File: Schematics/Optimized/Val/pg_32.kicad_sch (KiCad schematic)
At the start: 15 parts, among them U23 F04, U24 XALU32, U25 XALU32, U26 F51, U27 PA010, U30 PA011, U33 F04, U3607 F86, U3608 F04, U3613 F30, U3614 F30, U3615 F00, U3616 F04, U3617 F20, U3619 F20

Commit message: Polish
Tested: passed expmon_test_{typ,val} (-busmux)
Tested: passed run_udiag on r2000
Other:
- moved on the sheet: U23, U24, U25, U26, U27, U30, U33, U3607, U3608, U3613, U3614, U3615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

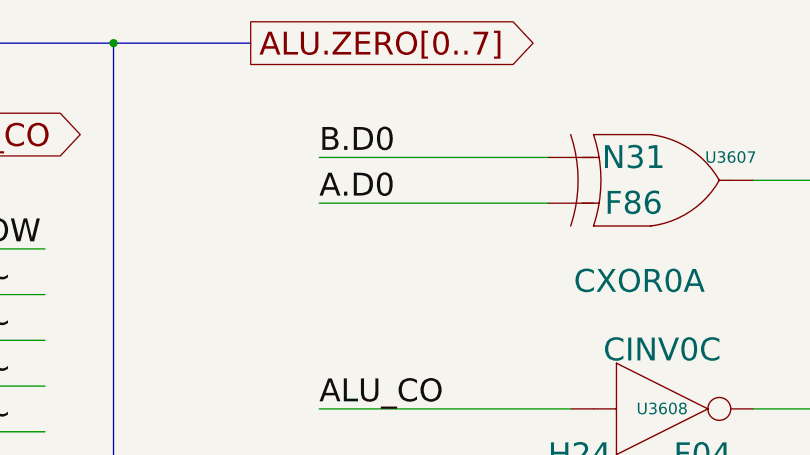
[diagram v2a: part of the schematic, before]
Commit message: Speedup: Condense multiplier, clocked parity comparison and more.
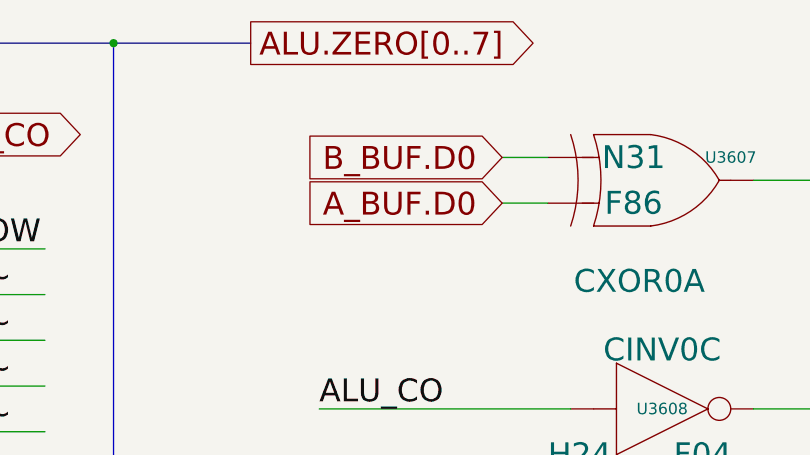
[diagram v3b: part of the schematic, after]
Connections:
- net A.D0: no longer U3607.2 (D1)
- net B.D0: no longer U3607.1 (D0)
- new net A_BUF.D0: U3607.2 (D1)
- new net B_BUF.D0: U3607.1 (D0)
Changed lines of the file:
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@@
     (stroke (width 0) (type default))
   )
-  (wire (pts (xy 302.26 27.94) (xy 327.66 27.94))
+  (wire (pts (xy 322.58 27.94) (xy 327.66 27.94))
     (stroke (width 0) (type default))
   )
@@
     (stroke (width 0) (type default))
   )
-  (wire (pts (xy 302.26 22.86) (xy 327.66 22.86))
+  (wire (pts (xy 322.58 22.86) (xy 327.66 22.86))
     (stroke (width 0) (type default))
   )
@@
     (effects (font (size 2.54 2.54)) (justify left bottom))
   )
-  (label "A.D0" (at 302.26 27.94 0) (fields_autoplaced)
-    (effects (font (size 2.54 2.54)) (justify left bottom))
-  )
   (label "A.D15" (at 66.04 104.14 0) (fields_autoplaced)
     (effects (font (size 2.54 2.54)) (justify left bottom))
@@
   )
   (label "ALU.ZERO3" (at 347.98 248.92 0) (fields_autoplaced)
-    (effects (font (size 2.54 2.54)) (justify left bottom))
-  )
-  (label "B.D0" (at 302.26 22.86 0) (fields_autoplaced)
     (effects (font (size 2.54 2.54)) (justify left bottom))
   )
@@
     )
   )
+  (global_label "B_BUF.D0" (shape input) (at 322.58 22.86 180) (fields_autoplaced)
+    (effects (font (size 2.54 2.54)) (justify right))
+    (property "Intersheetrefs" "${INTERSHEET_REFS}" (at 298.7477 22.86 0)
+      (effects (font (size 1.27 1.27)) (justify right))
+    )
+  )
   (global_label "ALU_CO" (shape output) (at 134.62 20.32 0) (fields_autoplaced)
     (effects (font (size 2.54 2.54)) (justify left))
@@
     )
   )
+  (global_label "A_BUF.D0" (shape input) (at 322.58 27.94 180) (fields_autoplaced)
+    (effects (font (size 2.54 2.54)) (justify right))
+    (property "Intersheetrefs" "${INTERSHEET_REFS}" (at 299.1106 27.94 0)
+      (effects (font (size 1.27 1.27)) (justify right))
+    )
+  )

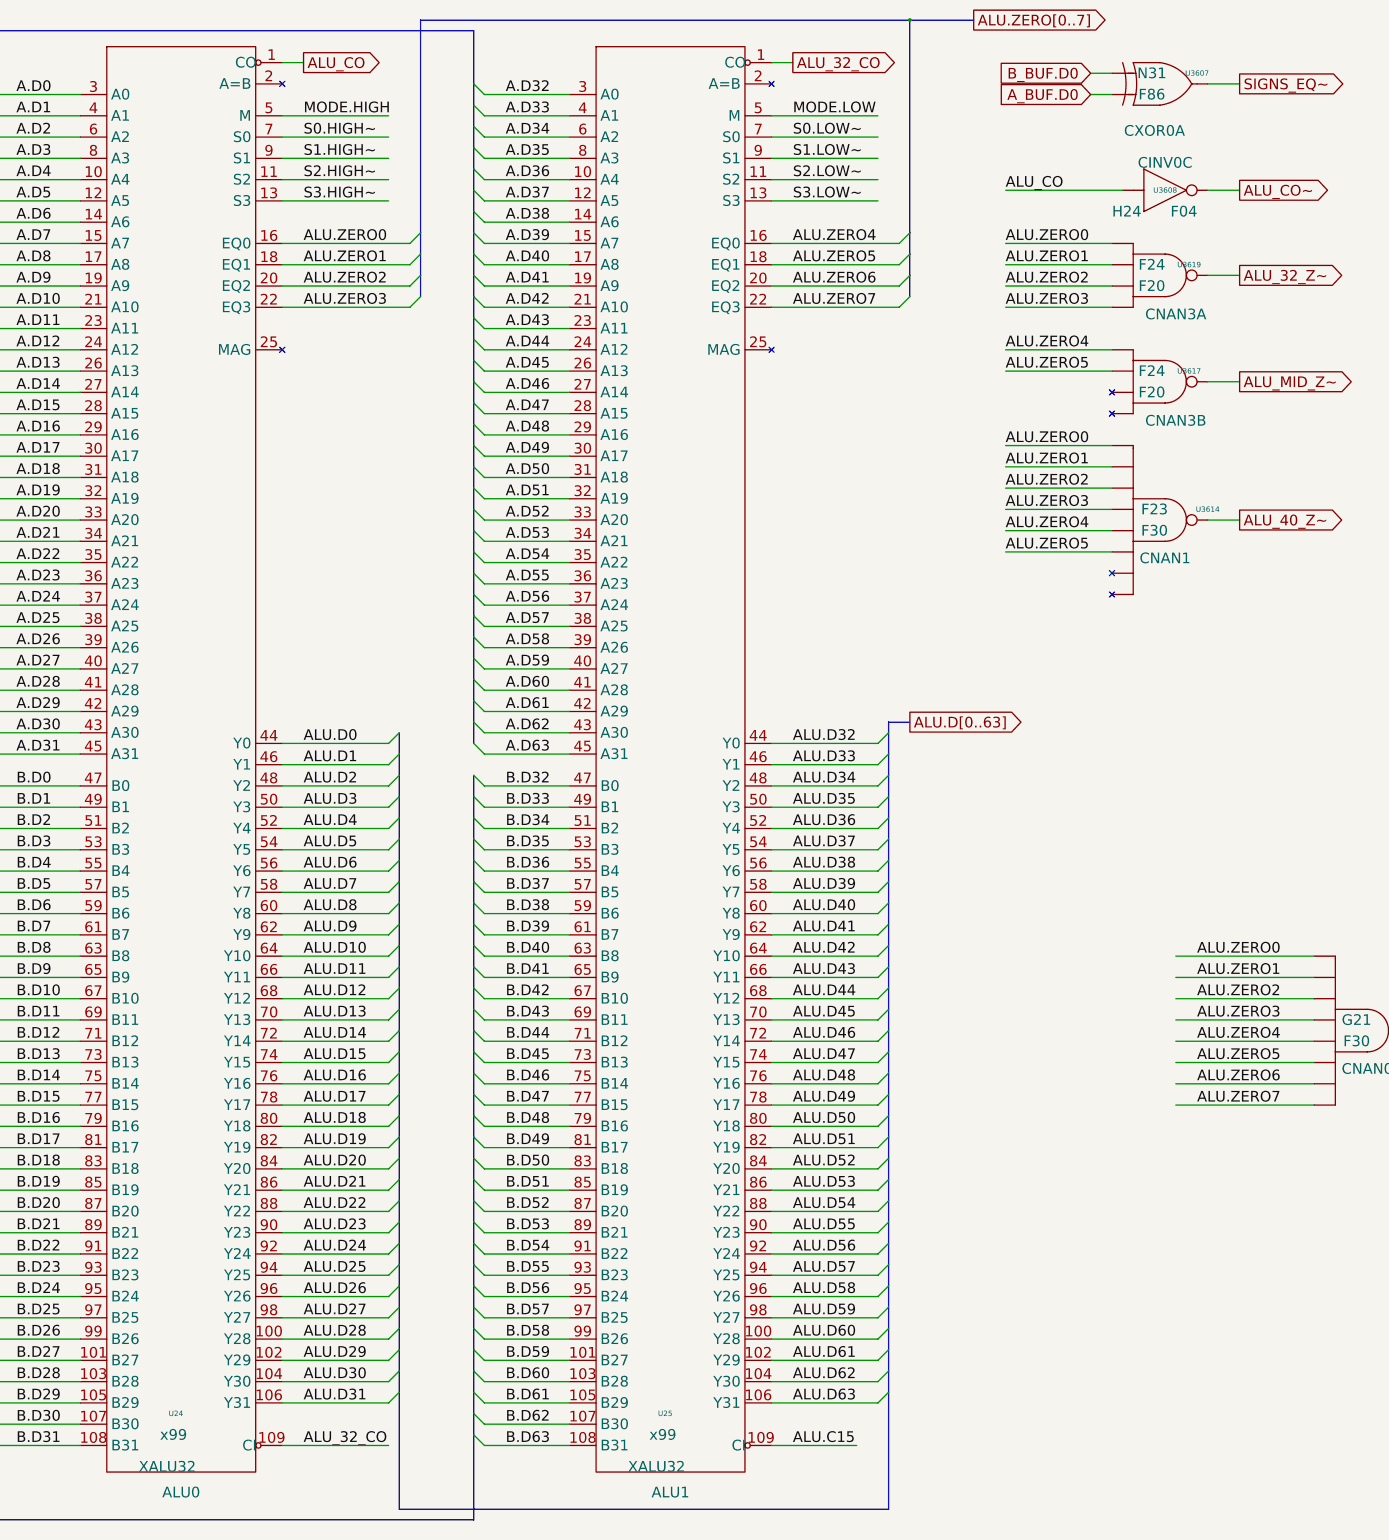
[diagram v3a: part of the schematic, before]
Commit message: Clock TYP & VAL ALU on Q2
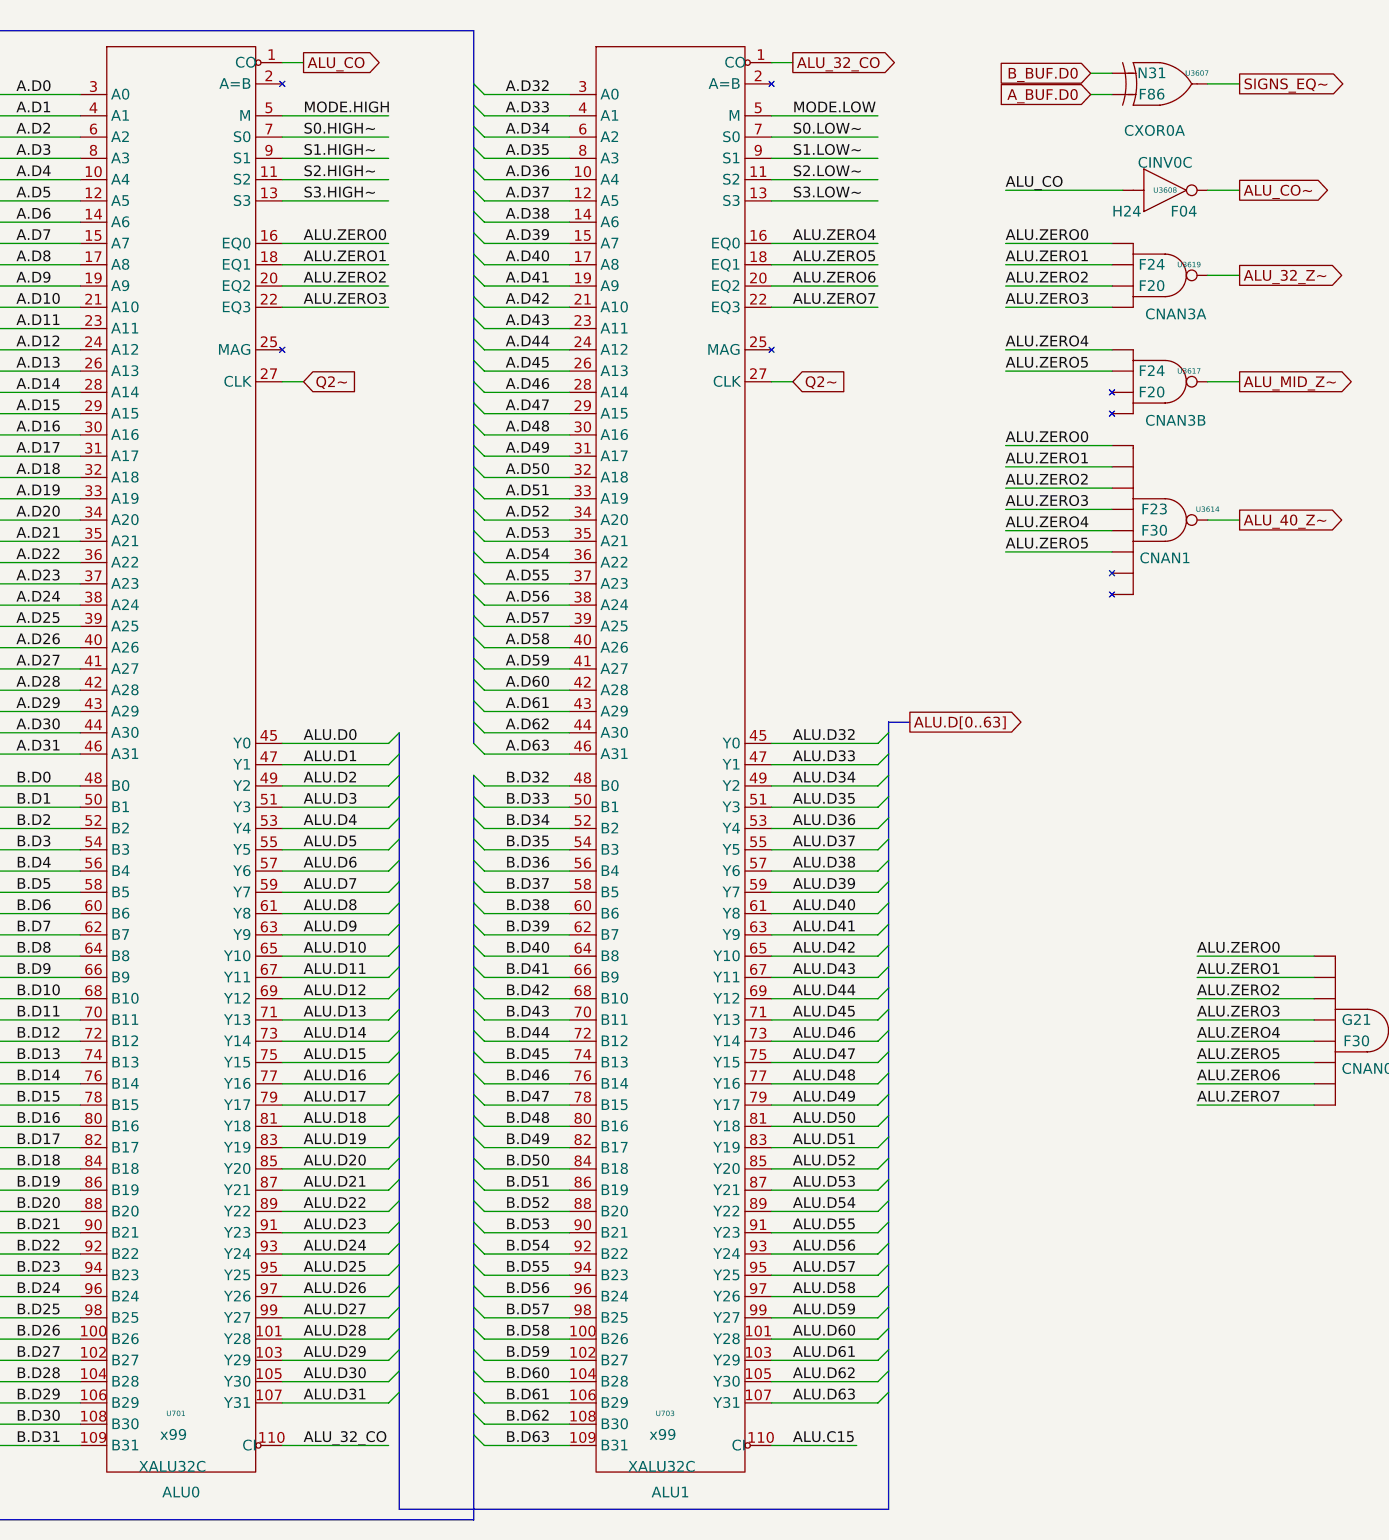
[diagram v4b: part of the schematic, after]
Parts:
- removed U24, U25: XALU32, symbol r1000:XALU32
- added U701, U703: XALU32C, symbol r1000:XALU32C
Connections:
- net A.D0: now also U701.3 (A0)
- net A.D1: now also U701.4 (A1)
- net A.D10: now also U701.21 (A10)
- net A.D11: now also U701.23 (A11)
- net A.D12: now also U701.24 (A12)
- net A.D13: now also U701.26 (A13)
- net A.D14: now also U701.28 (A14)
- net A.D15: now also U701.29 (A15)
- net A.D16: now also U701.30 (A16)
- net A.D17: now also U701.31 (A17)
- net A.D18: now also U701.32 (A18)
- net A.D19: now also U701.33 (A19)
- net A.D2: now also U701.6 (A2)
- net A.D20: now also U701.34 (A20)
- net A.D21: now also U701.35 (A21)
- net A.D22: now also U701.36 (A22)
- net A.D23: now also U701.37 (A23)
- net A.D24: now also U701.38 (A24)
- net A.D25: now also U701.39 (A25)
- net A.D26: now also U701.40 (A26)
- net A.D27: now also U701.41 (A27)
- net A.D28: now also U701.42 (A28)
- net A.D29: now also U701.43 (A29)
- net A.D3: now also U701.8 (A3)
- net A.D30: now also U701.44 (A30)
- net A.D31: now also U701.46 (A31)
- net A.D32: now also U703.3 (A0)
- net A.D33: now also U703.4 (A1)
- net A.D34: now also U703.6 (A2)
- net A.D35: now also U703.8 (A3)
- net A.D36: now also U703.10 (A4)
- net A.D37: now also U703.12 (A5)
- net A.D38: now also U703.14 (A6)
- net A.D39: now also U703.15 (A7)
- net A.D4: now also U701.10 (A4)
- net A.D40: now also U703.17 (A8)
- net A.D41: now also U703.19 (A9)
- net A.D42: now also U703.21 (A10)
- net A.D43: now also U703.23 (A11)
- net A.D44: now also U703.24 (A12)
- net A.D45: now also U703.26 (A13)
- net A.D46: now also U703.28 (A14)
- net A.D47: now also U703.29 (A15)
- net A.D48: now also U703.30 (A16)
- net A.D49: now also U703.31 (A17)
- net A.D5: now also U701.12 (A5)
- net A.D50: now also U703.32 (A18)
- net A.D51: now also U703.33 (A19)
- net A.D52: now also U703.34 (A20)
- net A.D53: now also U703.35 (A21)
- net A.D54: now also U703.36 (A22)
- net A.D55: now also U703.37 (A23)
- net A.D56: now also U703.38 (A24)
- net A.D57: now also U703.39 (A25)
- net A.D58: now also U703.40 (A26)
- net A.D59: now also U703.41 (A27)
- net A.D6: now also U701.14 (A6)
- net A.D60: now also U703.42 (A28)
- net A.D61: now also U703.43 (A29)
- net A.D62: now also U703.44 (A30)
- net A.D63: now also U703.46 (A31)
- net A.D7: now also U701.15 (A7)
- net A.D8: now also U701.17 (A8)
- net A.D9: now also U701.19 (A9)
- net ALU.C15: now also U703.110 (CI)
- net ALU.D0: now also U701.45 (Y0)
- net ALU.D1: now also U701.47 (Y1)
- net ALU.D10: now also U701.65 (Y10)
- net ALU.D11: now also U701.67 (Y11)
- net ALU.D12: now also U701.69 (Y12)
- net ALU.D13: now also U701.71 (Y13)
- net ALU.D14: now also U701.73 (Y14)
- net ALU.D15: now also U701.75 (Y15)
- net ALU.D16: now also U701.77 (Y16)
- net ALU.D17: now also U701.79 (Y17)
- net ALU.D18: now also U701.81 (Y18)
- net ALU.D19: now also U701.83 (Y19)
- net ALU.D2: now also U701.49 (Y2)
- net ALU.D20: now also U701.85 (Y20)
- net ALU.D21: now also U701.87 (Y21)
- net ALU.D22: now also U701.89 (Y22)
- net ALU.D23: now also U701.91 (Y23)
- net ALU.D24: now also U701.93 (Y24)
- net ALU.D25: now also U701.95 (Y25)
- net ALU.D26: now also U701.97 (Y26)
- net ALU.D27: now also U701.99 (Y27)
- net ALU.D28: now also U701.101 (Y28)
- net ALU.D29: now also U701.103 (Y29)
- net ALU.D3: now also U701.51 (Y3)
- net ALU.D30: now also U701.105 (Y30)
- net ALU.D31: now also U701.107 (Y31)
- net ALU.D32: now also U703.45 (Y0)
- net ALU.D33: now also U703.47 (Y1)
- net ALU.D34: now also U703.49 (Y2)
- net ALU.D35: now also U703.51 (Y3)
- net ALU.D36: now also U703.53 (Y4)
- net ALU.D37: now also U703.55 (Y5)
- net ALU.D38: now also U703.57 (Y6)
- net ALU.D39: now also U703.59 (Y7)
- net ALU.D4: now also U701.53 (Y4)
- net ALU.D40: now also U703.61 (Y8)
- net ALU.D41: now also U703.63 (Y9)
- net ALU.D42: now also U703.65 (Y10)
- net ALU.D43: now also U703.67 (Y11)
- net ALU.D44: now also U703.69 (Y12)
- net ALU.D45: now also U703.71 (Y13)
- net ALU.D46: now also U703.73 (Y14)
- net ALU.D47: now also U703.75 (Y15)
- net ALU.D48: now also U703.77 (Y16)
- net ALU.D49: now also U703.79 (Y17)
- net ALU.D5: now also U701.55 (Y5)
- net ALU.D50: now also U703.81 (Y18)
- net ALU.D51: now also U703.83 (Y19)
- net ALU.D52: now also U703.85 (Y20)
- net ALU.D53: now also U703.87 (Y21)
- net ALU.D54: now also U703.89 (Y22)
- net ALU.D55: now also U703.91 (Y23)
- net ALU.D56: now also U703.93 (Y24)
- net ALU.D57: now also U703.95 (Y25)
- net ALU.D58: now also U703.97 (Y26)
- net ALU.D59: now also U703.99 (Y27)
- net ALU.D6: now also U701.57 (Y6)
- net ALU.D60: now also U703.101 (Y28)
- net ALU.D61: now also U703.103 (Y29)
- net ALU.D62: now also U703.105 (Y30)
- net ALU.D63: now also U703.107 (Y31)
- net ALU.D7: now also U701.59 (Y7)
- net ALU.D8: now also U701.61 (Y8)
- net ALU.D9: now also U701.63 (Y9)
- net ALU.ZERO0: now also U701.16 (EQ0)
- net ALU.ZERO1: now also U701.18 (EQ1)
- net ALU.ZERO2: now also U701.20 (EQ2)
- net ALU.ZERO3: now also U701.22 (EQ3)
- net ALU.ZERO4: now also U703.16 (EQ0)
- net ALU.ZERO5: now also U703.18 (EQ1)
- net ALU.ZERO6: now also U703.20 (EQ2)
- net ALU.ZERO7: now also U703.22 (EQ3)
- net ALU_32_CO: now also U701.110 (CI), U703.1 (CO)
- net ALU_CO: now also U701.1 (CO)
- net B.D0: now also U701.48 (B0)
- net B.D1: now also U701.50 (B1)
- net B.D10: now also U701.68 (B10)
- net B.D11: now also U701.70 (B11)
- net B.D12: now also U701.72 (B12)
- net B.D13: now also U701.74 (B13)
- net B.D14: now also U701.76 (B14)
- net B.D15: now also U701.78 (B15)
- net B.D16: now also U701.80 (B16)
- net B.D17: now also U701.82 (B17)
- net B.D18: now also U701.84 (B18)
- net B.D19: now also U701.86 (B19)
- net B.D2: now also U701.52 (B2)
- net B.D20: now also U701.88 (B20)
- net B.D21: now also U701.90 (B21)
- net B.D22: now also U701.92 (B22)
- net B.D23: now also U701.94 (B23)
- net B.D24: now also U701.96 (B24)
- net B.D25: now also U701.98 (B25)
- net B.D26: now also U701.100 (B26)
- net B.D27: now also U701.102 (B27)
- net B.D28: now also U701.104 (B28)
- net B.D29: now also U701.106 (B29)
- net B.D3: now also U701.54 (B3)
- net B.D30: now also U701.108 (B30)
- net B.D31: now also U701.109 (B31)
- net B.D32: now also U703.48 (B0)
- net B.D33: now also U703.50 (B1)
- net B.D34: now also U703.52 (B2)
- net B.D35: now also U703.54 (B3)
- net B.D36: now also U703.56 (B4)
- net B.D37: now also U703.58 (B5)
- net B.D38: now also U703.60 (B6)
- net B.D39: now also U703.62 (B7)
- net B.D4: now also U701.56 (B4)
- net B.D40: now also U703.64 (B8)
- net B.D41: now also U703.66 (B9)
- net B.D42: now also U703.68 (B10)
- net B.D43: now also U703.70 (B11)
- net B.D44: now also U703.72 (B12)
- net B.D45: now also U703.74 (B13)
- net B.D46: now also U703.76 (B14)
- net B.D47: now also U703.78 (B15)
- net B.D48: now also U703.80 (B16)
- net B.D49: now also U703.82 (B17)
- net B.D5: now also U701.58 (B5)
- net B.D50: now also U703.84 (B18)
- net B.D51: now also U703.86 (B19)
- net B.D52: now also U703.88 (B20)
- net B.D53: now also U703.90 (B21)
- net B.D54: now also U703.92 (B22)
- net B.D55: now also U703.94 (B23)
- net B.D56: now also U703.96 (B24)
- net B.D57: now also U703.98 (B25)
- net B.D58: now also U703.100 (B26)
- net B.D59: now also U703.102 (B27)
- net B.D6: now also U701.60 (B6)
- net B.D60: now also U703.104 (B28)
- net B.D61: now also U703.106 (B29)
- net B.D62: now also U703.108 (B30)
- net B.D63: now also U703.109 (B31)
- net B.D7: now also U701.62 (B7)
- net B.D8: now also U701.64 (B8)
- net B.D9: now also U701.66 (B9)
- net MODE.HIGH: now also U701.5 (M)
- net MODE.LOW: now also U703.5 (M)
- net S0.HIGH~: now also U701.7 (S0)
- net S0.LOW~: now also U703.7 (S0)
- net S1.HIGH~: now also U701.9 (S1)
- net S1.LOW~: now also U703.9 (S1)
- net S2.HIGH~: now also U701.11 (S2)
- net S2.LOW~: now also U703.11 (S2)
- net S3.HIGH~: now also U701.13 (S3)
- net S3.LOW~: now also U703.13 (S3)
- new net Q2~: U701.27 (CLK), U703.27 (CLK)

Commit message: Condensation of SEQ, TYP & VAL conditions
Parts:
- removed U33, U3616: F04, symbol r1000:F04
- removed U3607: F86, symbol r1000:F86
- removed U3613, U3614: F30, symbol r1000:F30
- removed U3615: F00, symbol r1000:F00
- removed U3617, U3619: F20, symbol r1000:F20
- added GB164, GB166, GB172, GB176, GB178, GB181, GB182, GB183, GB185, GB186, GB187: GB, symbol r1000:GB
- added U3602, U3603: F86, symbol r1000:F86
- added U3604: F51, symbol r1000:F51
- added U3605: F74, symbol r1000:F74
- added U705: XVFCND, symbol r1000:XVFCND
- added U807: XVCOND, symbol r1000:XVCOND
- renumbered U3608 to U1705
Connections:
- net ALU.D0: now also U807.18 (C1C)
- net ALU.ZERO0: now also U705.17 (AZ0), U807.35 (AZ0)
- net ALU.ZERO1: now also U705.18 (AZ1), U807.36 (AZ1)
- net ALU.ZERO2: now also U705.19 (AZ2), U807.37 (AZ2)
- net ALU.ZERO3: now also U705.20 (AZ3), U807.38 (AZ3)
- net ALU.ZERO4: now also U705.21 (AZ4), U807.39 (AZ4)
- net ALU.ZERO5: now also U705.22 (AZ5), U807.40 (AZ5)
- net ALU.ZERO6: now also U705.23 (AZ6), U807.41 (AZ6)
- net ALU.ZERO7: now also U705.24 (AZ7), U807.42 (AZ7)
- net ALU_32_CO: now also U807.15 (C0H)
- net ALU_CO: now also U3604.5 (B2), U705.15 (ACO), U807.16 (C1A)
- net ALU_CO~: now also U3602.2 (D1)
- net A_BUF.D0: now also U705.13 (BAD0), U807.21 (BAD0)
- net B_BUF.D0: now also U705.14 (BBD0), U807.22 (BBD0)
- net DIVIDE: now also U3604.3 (A3)
- net DIVIDE~: now also U3604.6 (B3)
- net IS_BINARY: now also U807.23 (ISBN)
- net LAST_VAL~: now also U705.16 (LVAL), U807.19 (C1H), U807.9 (LVCND)
- net OVR.EN~: now also U807.17 (OVRE)
- net SUB_ELSE_ADD~: now also U807.24 (SELA)
- net V.Q_BIT~: now also GB164.1, U3603.1 (D0), U3605.5 (Q), U807.20 (C2D)
- new net: U3602.3 (Q), U3603.2 (D1)
- new net: U3603.3 (Q), U3604.1 (A1)
- new net: U3604.7 (Q), U3605.2 (D)
- new net COND~.SCLK: U3605.3 (CLK), U807.14 (SCLK)
- new net FIU_COND: U705.9 (FCOND)
- new net FIU_COND.SEL0: U705.2 (FCSEL0)
- new net FIU_COND.SEL1: U705.4 (FCSEL1)
- new net FIU_COND.SEL2: U705.6 (FCSEL2)
- new net LOOP_CNT0: U807.25 (LCN0)
- new net LOOP_CNT1: U807.26 (LCN1)
- new net LOOP_CNT2: U807.27 (LCN2)
- new net LOOP_CNT3: U807.28 (LCN3)
- new net LOOP_CNT4: U807.29 (LCN4)
- new net LOOP_CNT5: U807.30 (LCN5)
- new net LOOP_CNT6: U807.31 (LCN6)
- new net LOOP_CNT7: U807.32 (LCN7)
- new net LOOP_CNT8: U807.33 (LCN8)
- new net LOOP_CNT9: U807.34 (LCN9)
- new net M_BIT~: U3602.1 (D0), U807.12 (MBIT)
- new net SNEAK.EN~: U705.12 (SNK)
- new net V.COND.SEL0: GB166.1, U705.1 (SEL0), U807.1 (SEL0)
- new net V.COND.SEL1: GB172.1, U705.3 (SEL1), U807.3 (SEL1)
- new net V.COND.SEL2: GB176.1, U705.5 (SEL2), U807.5 (SEL2)
- new net V.COND.SEL3: GB178.1, U705.7 (SEL3), U807.7 (SEL3)
- new net V.COND.SEL4: GB181.1, U705.8 (SEL4), U807.8 (SEL4)
- new net V.COND.SEL5: GB182.1, U705.10 (SEL5), U807.10 (SEL5)
- new net V.COND.SEL6: GB183.1, U705.11 (SEL6), U807.11 (SEL6)
- new net V.COND.VAL0: GB185.1, U807.2 (VCOND0)
- new net V.COND.VAL1: GB186.1, U807.4 (VCOND1)
- new net V.COND.VAL2: GB187.1, U807.6 (VCOND2)
- no-connect marks 12 -> 14
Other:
- moved on the sheet: U1705, U23, U26, U27, U30

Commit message: Typ/Val/Mem32 improvements
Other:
- moved on the sheet: GB166, GB172, GB176, GB178, GB181, GB182, GB183, GB185, GB186, GB187, U1705, U23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
